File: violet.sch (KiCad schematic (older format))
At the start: 27 parts, among them J1 NEIGHBOR1, J2 NEIGHBOR2, J7 BONUS_ROW

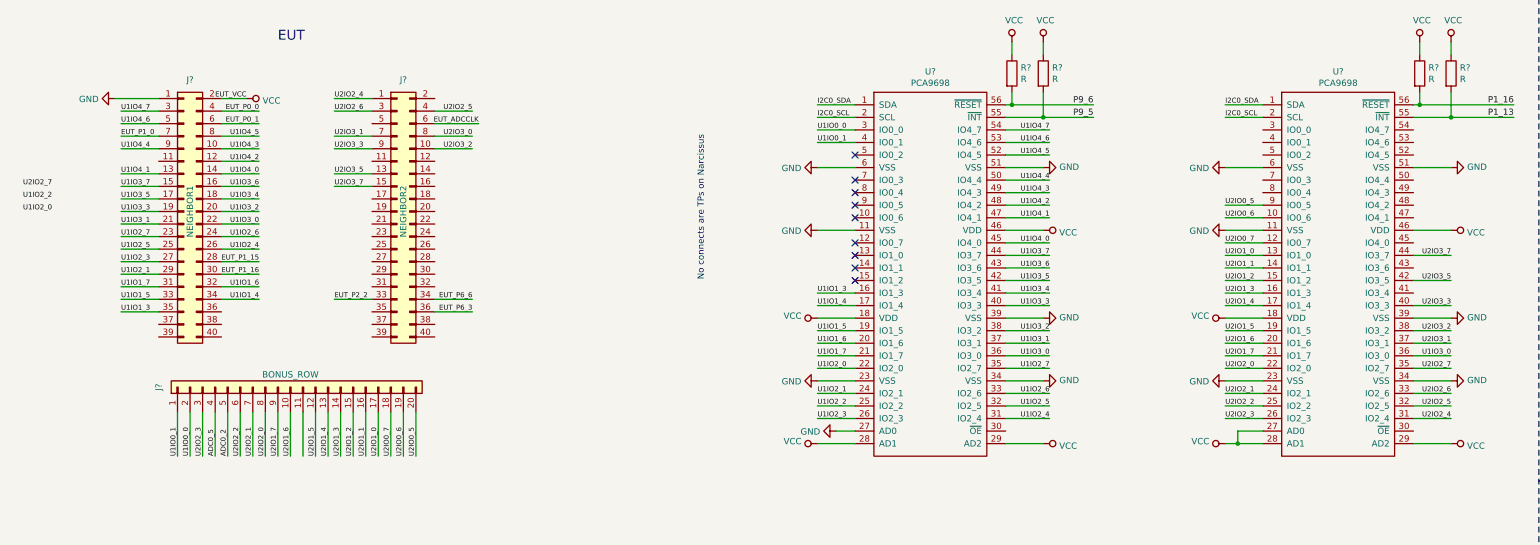
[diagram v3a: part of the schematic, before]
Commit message: Add more labels; fix label nomenclature
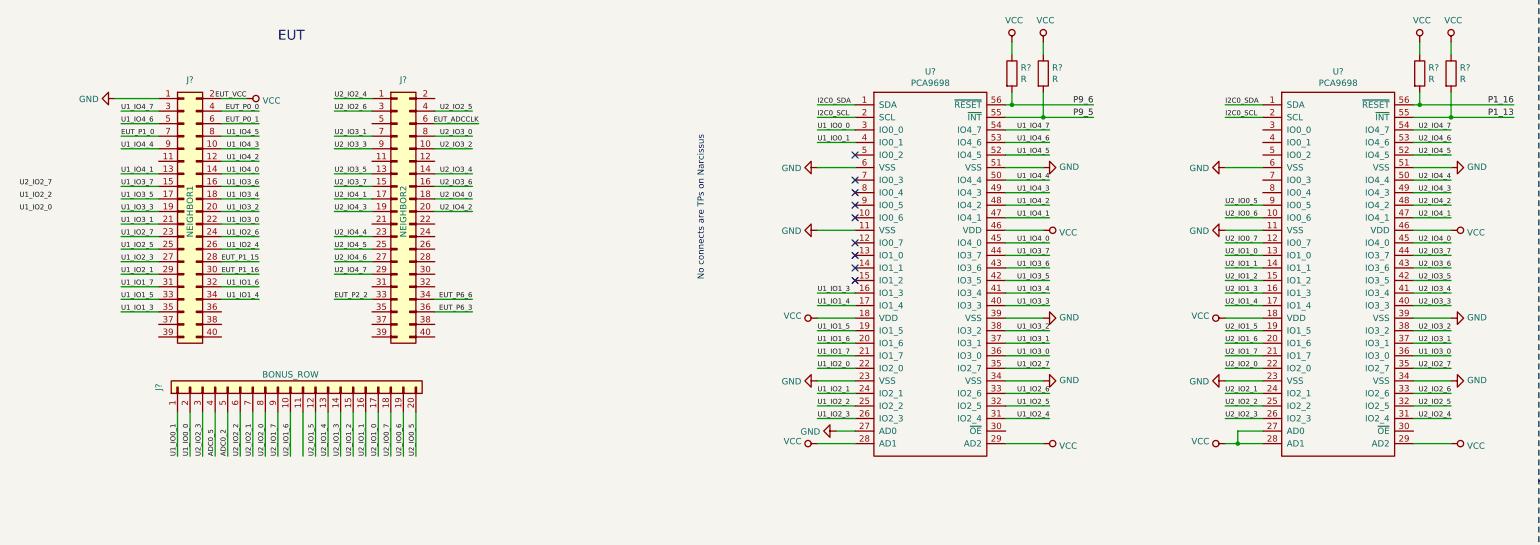
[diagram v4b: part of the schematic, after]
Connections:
- net U2_IO3_4: now reaches J?.14 (Pin_14)
- net U2_IO3_4: now also U?.41 (IO3_4)
- net U2_IO3_6: now reaches J?.16 (Pin_16)
- net U2_IO3_6: now also U?.43 (IO3_6)
- net U2_IO4_1: now reaches J?.17 (Pin_17)
- net U2_IO4_1: now also U?.47 (IO4_1)
- net U2_IO4_0: now reaches J?.18 (Pin_18)
- net U2_IO4_0: now also U?.45 (IO4_0)
- net U2_IO4_3: now reaches J?.19 (Pin_19)
- net U2_IO4_3: now also U?.49 (IO4_3)
- net U2_IO4_2: now reaches J?.20 (Pin_20)
- net U2_IO4_2: now also U?.48 (IO4_2)
- net U2_IO4_4: now reaches J?.23 (Pin_23)
- net U2_IO4_4: now also U?.50 (IO4_4)
- net U2_IO4_5: now reaches J?.25 (Pin_25)
- net U2_IO4_5: now also U?.52 (IO4_5)
- net U2_IO4_6: now reaches J?.27 (Pin_27)
- net U2_IO4_6: now also U?.53 (IO4_6)
- net U2_IO4_7: now reaches J?.29 (Pin_29)
- net U2_IO4_7: now also U?.54 (IO4_7)
- net U1IO0_0 renamed U1_IO0_0
- net U1IO0_1 renamed U1_IO0_1
- net U1IO1_3 renamed U1_IO1_3
- net U1IO1_4 renamed U1_IO1_4
- net U1IO1_5 renamed U1_IO1_5
- net U1IO1_6 renamed U1_IO1_6
- net U1IO1_7 renamed U1_IO1_7
- net U1IO2_0 renamed U1_IO2_0
- net U1IO2_1 renamed U1_IO2_1
- net U1IO2_2 renamed U1_IO2_2
- net U1IO2_3 renamed U1_IO2_3
- net U1IO2_4 renamed U1_IO2_4
- net U1IO2_5 renamed U1_IO2_5
- net U1IO2_6 renamed U1_IO2_6
- net U1IO2_7 renamed U1_IO2_7
- net U1IO3_0 renamed U1_IO3_0
- net U1IO3_1 renamed U1_IO3_1
- net U1IO3_2 renamed U1_IO3_2
- net U1IO3_3 renamed U1_IO3_3
- net U1IO3_4 renamed U1_IO3_4
- net U1IO3_5 renamed U1_IO3_5
- net U1IO3_6 renamed U1_IO3_6
- net U1IO3_7 renamed U1_IO3_7
- net U1IO4_0 renamed U1_IO4_0
- net U1IO4_1 renamed U1_IO4_1
- net U1IO4_2 renamed U1_IO4_2
- net U1IO4_3 renamed U1_IO4_3
- net U1IO4_4 renamed U1_IO4_4
- net U1IO4_5 renamed U1_IO4_5
- net U1IO4_6 renamed U1_IO4_6
- net U1IO4_7 renamed U1_IO4_7
- net U2IO0_5 renamed U2_IO0_5
- net U2IO0_6 renamed U2_IO0_6
- net U2IO0_7 renamed U2_IO0_7
- net U2IO1_0 renamed U2_IO1_0
- net U2IO1_1 renamed U2_IO1_1
- net U2IO1_2 renamed U2_IO1_2
- net U2IO1_3 renamed U2_IO1_3
- net U2IO1_4 renamed U2_IO1_4
- net U2IO1_5 renamed U2_IO1_5
- net U2IO1_6 renamed U2_IO1_6
- net U2IO1_7 renamed U2_IO1_7
- net U2IO2_0 renamed U2_IO2_0
- net U2IO2_1 renamed U2_IO2_1
- net U2IO2_2 renamed U2_IO2_2
- net U2IO2_3 renamed U2_IO2_3
- net U2IO2_4 renamed U2_IO2_4
- net U2IO2_5 renamed U2_IO2_5
- net U2IO2_6 renamed U2_IO2_6
- net U2IO2_7 renamed U2_IO2_7
- net U2IO3_0 renamed U2_IO3_0
- net U2IO3_1 renamed U2_IO3_1
- net U2IO3_2 renamed U2_IO3_2
- net U2IO3_3 renamed U2_IO3_3
- net U2IO3_5 renamed U2_IO3_5
- net U2IO3_7 renamed U2_IO3_7

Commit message: Add more labels; add another I/O expander
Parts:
- added U?: PCA9674, symbol gsg-symbols:PCA9674
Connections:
- net GND: now also U?.2 (AD1), U?.3 (AD2), U?.8 (VSS)
- net I2C0_SCL: now also J?.40 (Pin_40), U?.14 (SCL)
- net I2C0_SDA: now also J?.39 (Pin_39), U?.15 (SDA)
- net U1_IO2_0: now also J?.39 (Pin_39)
- net U1_IO2_2: now also J?.37 (Pin_37)
- net U2_IO2_7: now also J?.28 (Pin_28)
- net VCC: now also U?.1 (AD0)
- net U1_IO0_7: now reaches J?.11 (Pin_11)
- net U1_IO0_7: now also U?.12 (IO0_7)
- net U1_IO1_2: now reaches J?.12 (Pin_12)
- net U1_IO1_2: now also U?.15 (IO1_2)
- net U1_IO1_0: now reaches J?.21 (Pin_21)
- net U1_IO1_0: now also U?.13 (IO1_0)
- net U2_IO0_1: now reaches J?.22 (Pin_22)
- net U2_IO0_1: now also U?.4 (IO0_1)
- net U2_IO0_2: now reaches J?.24 (Pin_24)
- net U2_IO0_2: now also J?.11 (Pin_11), U?.5 (IO0_2)
- net U2_IO0_3: now reaches J?.26 (Pin_26)
- net U2_IO0_3: now also U?.7 (IO0_3)
- net U2_IO0_0: now reaches J?.31 (Pin_31)
- net U2_IO0_0: now also U?.3 (IO0_0)
- net U2_IO0_4: now reaches J?.35 (Pin_35)
- net U2_IO0_4: now also U?.8 (IO0_4)
- net U1_IO1_1: now reaches J?.37 (Pin_37)
- net U1_IO1_1: now also U?.14 (IO1_1)
- net U1_IO0_6: now reaches J?.5 (Pin_5)
- net U1_IO0_6: now also U?.10 (IO0_6)
- net U1_IO0_3: now reaches J?.36 (Pin_36)
- net U1_IO0_3: now also U?.7 (IO0_3)
- net U1_IO0_4: now reaches J?.38 (Pin_38)
- net U1_IO0_4: now also U?.8 (IO0_4)
- net U1_IO0_5: now reaches J?.40 (Pin_40)
- net U1_IO0_5: now also U?.9 (IO0_5)
- net U1_IO0_2: now reaches U?.5 (IO0_2)
- no-connect marks 151 -> 142
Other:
- note removed: "No connects are TPs on Narcissus"
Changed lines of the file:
@@
 	3150 4300 3150 3950
-Wire Wire Line
-	3050 4300 3050 3950
 Wire Wire Line
 	2850 4300 2850 3950
@@
 Wire Wire Line
 	2100 8750 1500 8750
-$Comp
-L gsg-symbols:PCA9698 U?
-U 1 1 5F510C18
-P 8050 2850
-F 0 "U?" H 8050 4465 50  0000 C CNN
-F 1 "PCA9698" H 8050 4374 50  0000 C CNN
-F 2 "" H 8050 2850 40  0000 C CNN
-F 3 "" H 8050 2850 40  0000 C CNN
-	1    8050 2850
-	1    0    0    -1
-$EndComp
 $Comp
 L gsg-symbols:PCA9698 U?
@@
 Text Label 12700 1600 2    50   ~ 0
 P1_13
-NoConn ~ 7450 2700
-NoConn ~ 7450 2600
-NoConn ~ 7450 2400
-NoConn ~ 7450 2100
-NoConn ~ 7450 2300
-NoConn ~ 7450 2900
-NoConn ~ 7450 2800
-NoConn ~ 7450 2200
-NoConn ~ 7450 1900
-Text Notes 6250 2900 1    50   ~ 0
-No connects are TPs on Narcissus
 Text Label 15100 6700 0    40   ~ 0
 P2_8
@@
 Text Label 2700 2650 2    40   ~ 0
 U1_IO2_4
-Text Label 1050 2250 2    40   ~ 0
-U1_IO2_2
-Text Label 1050 2350 2    40   ~ 0
-U1_IO2_0
 Wire Wire Line
 	8650 3600 9000 3600
@@
 Text Label 4400 1550 2    40   ~ 0
 U2_IO2_5
-Text Label 1050 2150 2    40   ~ 0
+Text Label 4400 2750 2    40   ~ 0
 U2_IO2_7
 Wire Wire Line
@@
 Text Label 12200 1700 2    40   ~ 0
 U2_IO4_7
+Text Label 3050 4300 1    50   ~ 0
+I\O
+Text Label 4600 1450 2    40   ~ 0
+EUT_+5V
+Wire Wire Line
+	3300 2950 3600 2950
+Wire Wire Line
+	3300 3150 3600 3150
+Text Label 3300 2950 0    40   ~ 0
+U2_IO0_0
+Text Label 3300 3150 0    40   ~ 0
+U2_IO0_4
+Wire Wire Line
+	10400 1700 10700 1700
+Wire Wire Line
+	10400 1900 10700 1900
+Wire Wire Line
+	10400 2200 10700 2200
+Text Label 10400 1700 0    40   ~ 0
+U2_IO0_0
+Text Label 10400 1900 0    40   ~ 0
+U2_IO0_2
+Text Label 10400 2200 0    40   ~ 0
+U2_IO0_4
+Text Label 4250 2850 0    40   ~ 0
+I\O
+Text Label 4250 2950 0    40   ~ 0
+I\O
+Text Label 4250 3250 0    40   ~ 0
+I\O
+Text Label 3300 3350 0    40   ~ 0
+I2C0_SDA
+Wire Wire Line
+	3600 3350 3300 3350
+Text Label 4400 3350 2    40   ~ 0
+I2C0_SCL
+Wire Wire Line
+	4400 3350 4100 3350
+$Comp
+L power:GND #PWR?
+U 1 1 604CCBF3
+P 11050 5700
+F 0 "#PWR?" H 11050 5450 50  0001 C CNN
+F 1 "GND" V 11055 5572 50  0000 R CNN
+F 2 "" H 11050 5700 50  0001 C CNN
+F 3 "" H 11050 5700 50  0001 C CNN
+	1    11050 5700
+	0    1    1    0
+$EndComp
+Wire Wire Line
+	11350 5700 11050 5700
+Wire Wire Line
+	1600 1950 1900 1950
+Text Label 4400 2650 2    40   ~ 0
+U2_IO0_3
+Text Label 4400 2450 2    40   ~ 0
+U2_IO0_1
+Text Label 1600 3350 0    40   ~ 0
+U1_IO2_0
+Text Label 1600 3250 0    40   ~ 0
+U1_IO2_2
+Text Label 4400 2550 2    40   ~ 0
+U2_IO0_2
+Wire Wire Line
+	1600 3250 1900 3250
+Wire Wire Line
+	1600 3350 1900 3350
+$Comp
+L gsg-symbols:PCA9698 U?
+U 1 1 5F510C18
+P 8050 2850
+F 0 "U?" H 8050 4465 50  0000 C CNN
+F 1 "PCA9698" H 8050 4374 50  0000 C CNN
+F 2 "" H 8050 2850 40  0000 C CNN
+F 3 "" H 8050 2850 40  0000 C CNN
+	1    8050 2850
+	1    0    0    -1
+$EndComp
+Wire Wire Line
+	7150 1900 7450 1900
+Wire Wire Line
+	7150 2100 7450 2100
+Wire Wire Line
+	7150 2200 7450 2200
+Wire Wire Line
+	7150 2300 7450 2300
+Wire Wire Line
+	7150 2400 7450 2400
+Wire Wire Line
+	7150 2600 7450 2600
+Wire Wire Line
+	7150 2700 7450 2700
+Wire Wire Line
+	7150 2800 7450 2800
+Wire Wire Line
+	7150 2900 7450 2900
+Text Label 7150 1900 0    40   ~ 0
+U1_IO0_2
+Text Label 1600 1950 0    40   ~ 0
+U2_IO0_2
+Wire Wire Line
+	2700 3150 2400 3150
+Wire Wire Line
+	2700 3250 2400 3250
+Wire Wire Line
+	2700 3350 2400 3350
+Text Label 7150 2100 0    40   ~ 0
+U1_IO0_3
+Text Label 7150 2200 0    40   ~ 0
+U1_IO0_4
+Text Label 7150 2300 0    40   ~ 0
+U1_IO0_5
+Text Label 2700 3150 2    40   ~ 0
+U1_IO0_3
+Text Label 2700 3250 2    40   ~ 0
+U1_IO0_4
+Text Label 2700 3350 2    40   ~ 0
+U1_IO0_5
+Wire Wire Line
+	3300 1650 3600 1650
+Wire Wire Line
+	3300 1950 3600 1950
+Wire Wire Line
+	3300 2450 3600 2450
+Text Label 7150 2400 0    40   ~ 0
+U1_IO0_6
+Text Label 7150 2600 0    40   ~ 0
+U1_IO0_7
+Text Label 7150 2700 0    40   ~ 0
+U1_IO1_0
+Text Label 3300 1650 0    40   ~ 0
+U1_IO0_6
+Text Label 3300 1950 0    40   ~ 0
+U1_IO0_7
+Text Label 3300 2450 0    40   ~ 0
+U1_IO1_0
+Wire Wire Line
+	3300 3250 3600 3250
+Text Label 7150 2800 0    40   ~ 0
+U1_IO1_1
+Text Label 3300 3250 0    40   ~ 0
+U1_IO1_1
+Wire Wire Line
+	4400 1950 4100 1950
+Text Label 7150 2900 0    40   ~ 0
+U1_IO1_2
+Text Label 4400 1950 2    40   ~ 0
+U1_IO1_2
+Wire Wire Line
+	4400 2450 4100 2450
+Wire Wire Line
+	4400 2550 4100 2550
+Wire Wire Line
+	4400 2650 4100 2650
+Wire Wire Line
+	4400 2750 4100 2750
+Wire Wire Line
+	10400 1800 10700 1800
+Wire Wire Line
+	10400 2100 10700 2100
+Text Label 10400 1800 0    40   ~ 0
+U2_IO0_1
+Text Label 10400 2100 0    40   ~ 0
+U2_IO0_3
+$Comp
+L gsg-symbols:PCA9674 U?
+U 1 1 6124F8C7
+P 11800 5350
+F 0 "U?" H 11800 5902 40  0000 C CNN
+F 1 "PCA9674" H 11800 5826 40  0000 C CNN
+F 2 "" H 11800 5350 40  0000 C CNN
+F 3 "" H 11800 5350 40  0000 C CNN
+	1    11800 5350
+	1    0    0    -1
+$EndComp
+Wire Wire Line
+	12550 5200 12250 5200
+Text Label 12550 5200 2    40   ~ 0
+I2C0_SCL
+Wire Wire Line
+	12250 5100 12550 5100
+Text Label 12550 5100 2    40   ~ 0
+I2C0_SDA
+$Comp
+L power:GND #PWR?
+U 1 1 61412BAB
+P 11050 5200
+F 0 "#PWR?" H 11050 4950 50  0001 C CNN
+F 1 "GND" V 11055 5072 50  0000 R CNN
+F 2 "" H 11050 5200 50  0001 C CNN
+F 3 "" H 11050 5200 50  0001 C CNN
+	1    11050 5200
+	0    1    1    0
+$EndComp
+Wire Wire Line
+	11350 5200 11150 5200
+Wire Wire Line
+	11350 5100 11150 5100
+Wire Wire Line
+	11150 5100 11150 5200
+Connection ~ 11150 5200
+Wire Wire Line
+	11150 5200 11050 5200
+$Comp
+L power:VCC #PWR?
+U 1 1 614CF790
+P 11050 5000
+F 0 "#PWR?" H 11050 4850 50  0001 C CNN
+F 1 "VCC" V 11068 5127 50  0000 L CNN
+F 2 "" H 11050 5000 50  0001 C CNN
+F 3 "" H 11050 5000 50  0001 C CNN
+	1    11050 5000
+	0    -1   -1   0
+$EndComp
+Wire Wire Line
+	11350 5000 11050 5000
 $EndSCHEMATC

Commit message: Add remaining labels; configure third I/O expander; add decoupling caps
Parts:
- added C? (x7): C, symbol Device:C
- added R? (x3): R, symbol Device:R
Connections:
- net GND: now also C?.1, C?.2, C?.2, C?.2, C?.2, C?.2, C?.2
- net P1_11: now also U?.30 (~OE~), R?.2
- net P1_15: now also U?.13 (INT), R?.2
- net P1_17: now also U?.30 (~OE~), R?.2
- net VCC: now also U?.16 (VDD), C?.1, C?.1, C?.1, C?.1, C?.1, C?.1, C?.2, R?.1, R?.1, R?.1
- net U3_IO_P4: now reaches J?.2 (Pin_2)
- net U3_IO_P4: now also U?.9 (P4)
- net U3_IO_P0: now reaches J?.30 (Pin_30)
- net U3_IO_P0: now also U?.4 (P0)
- net U3_IO_P1: now reaches J?.32 (Pin_32)
- net U3_IO_P1: now also U?.5 (P1)
- net U3_IO_P2: now reaches J?.38 (Pin_38)
- net U3_IO_P2: now also U?.6 (P2)
- net U3_IO_P3: now reaches J?.11 (Pin_11)
- net U3_IO_P3: now also U?.7 (P3)
- no-connect marks 142 -> 168
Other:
- note added: "???"
- moved on the sheet: R?, U?

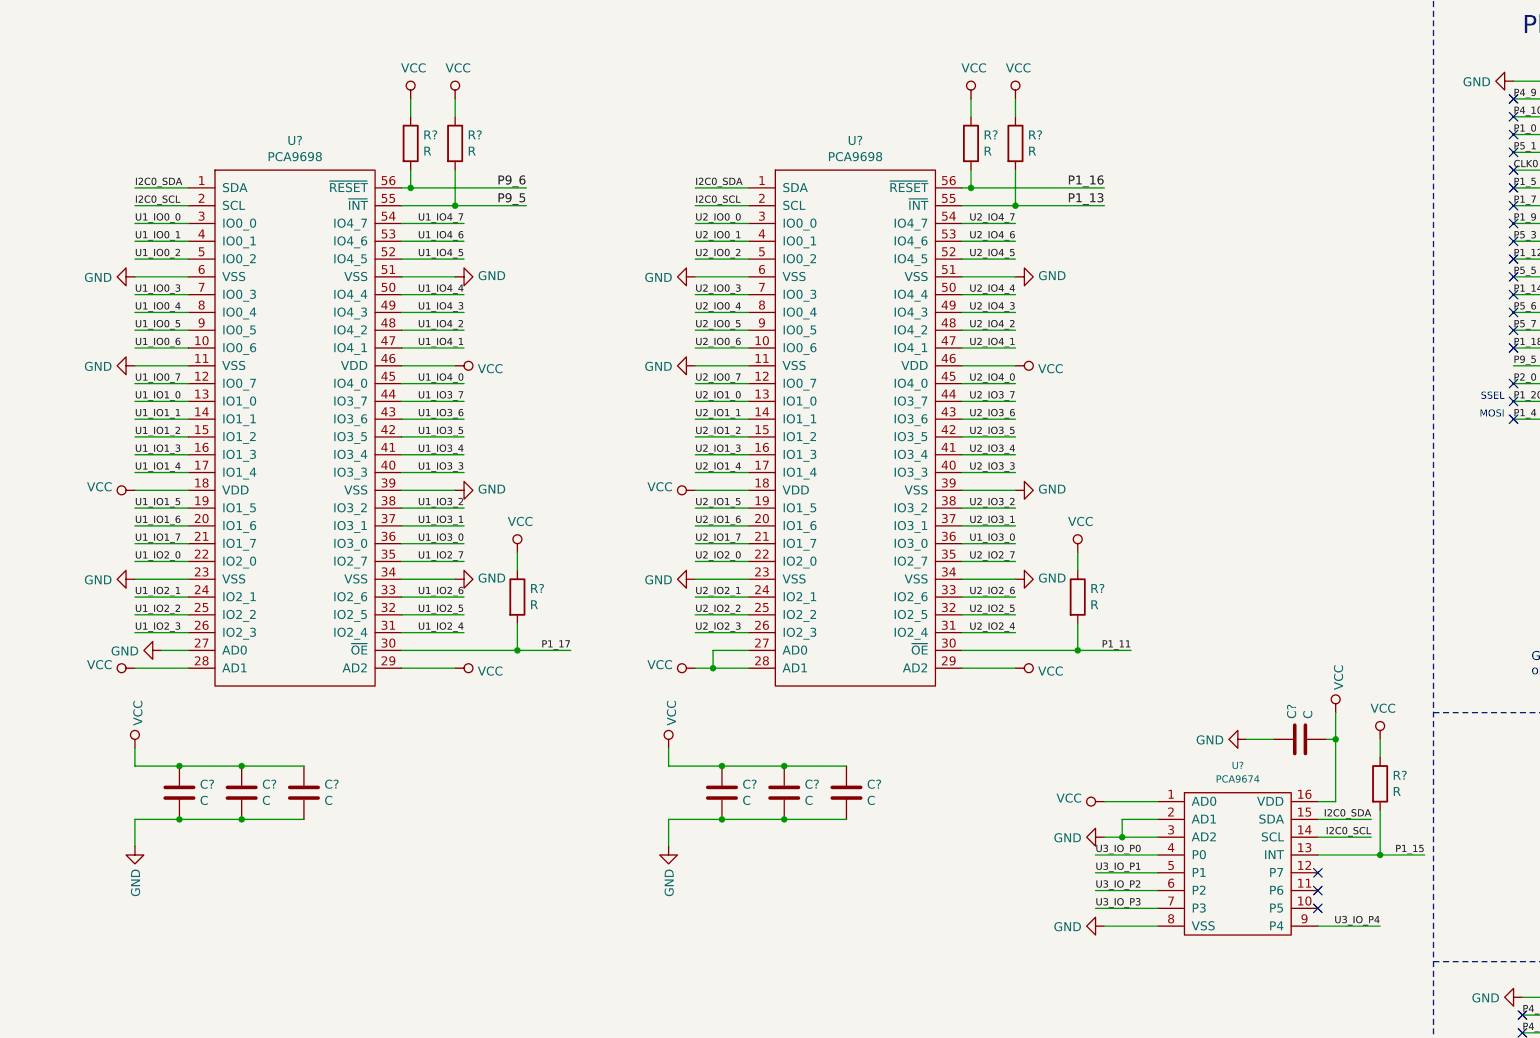
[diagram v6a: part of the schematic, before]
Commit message: Add parts and footprints
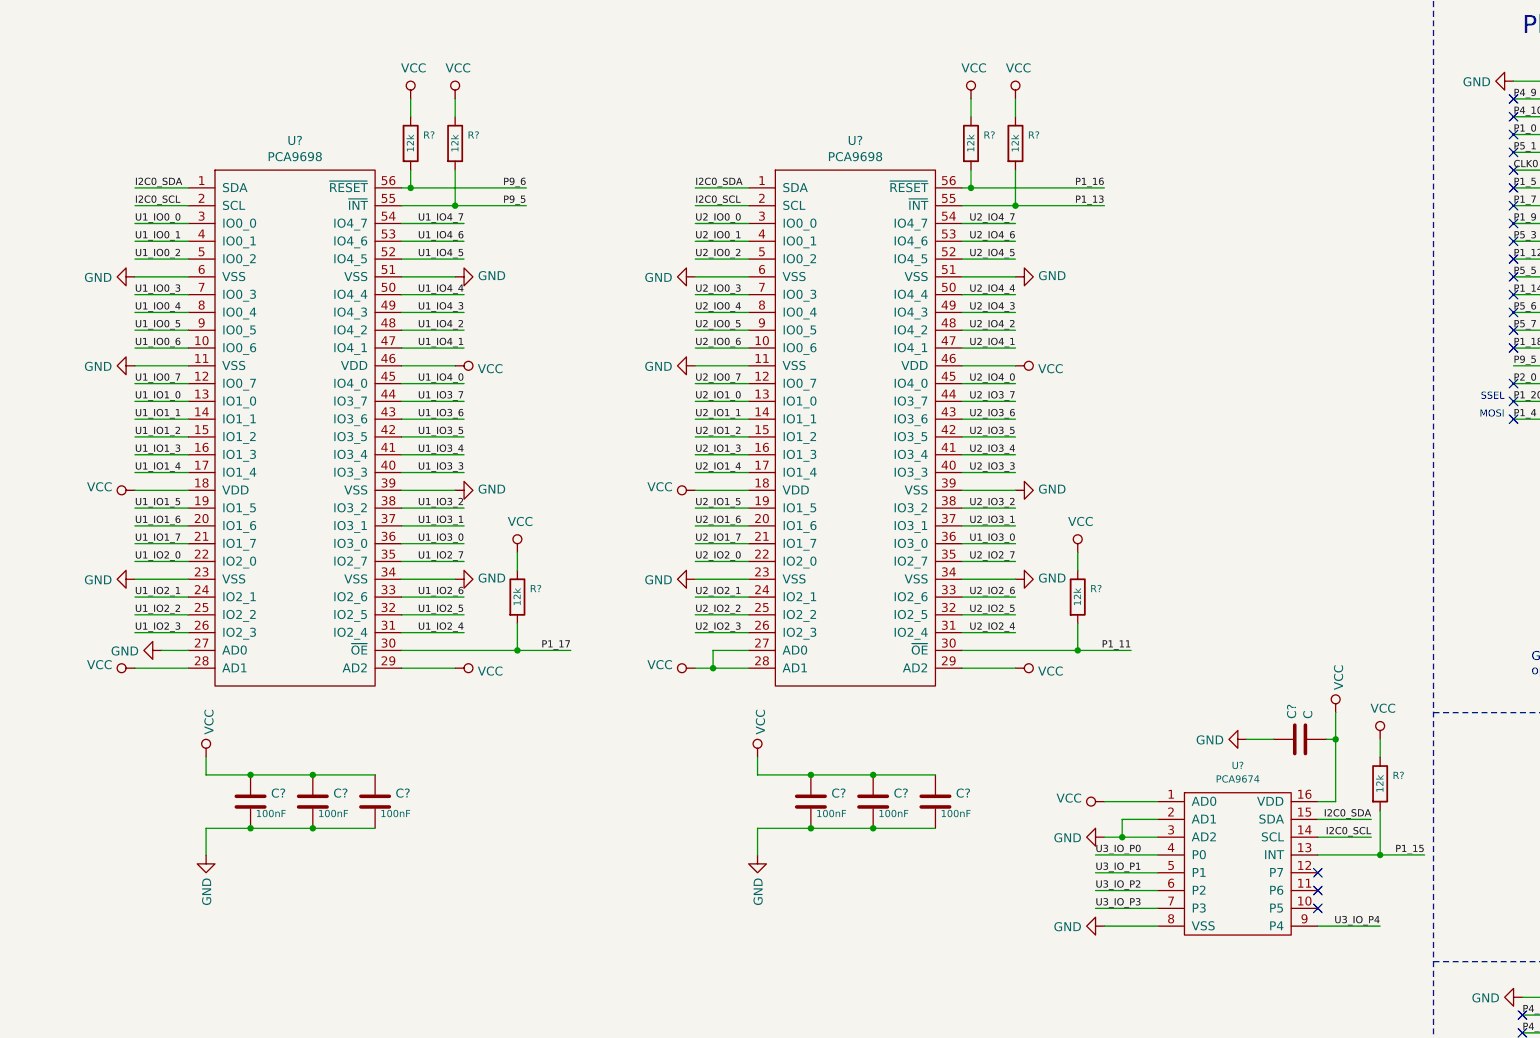
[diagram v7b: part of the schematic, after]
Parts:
- removed C? (x5): C, symbol Device:C
- removed R? (x6): R, symbol Device:R
- added C? (x5): 100nF, gsg-modules:0603, symbol Device:C
- added R? (x6): 12k, gsg-modules:0603, symbol Device:R
- C?: value C -> 100nF; footprint (none) -> gsg-modules:0603; Description (none) -> CAP CER 0.1UF 16V X7R 0603; Manufacturer (none) -> KEMET; Part Number (none) -> C0603C104M4RACTU
- R?: value R -> 12k; footprint (none) -> gsg-modules:0603; Description (none) -> RES 12K OHM 1% 1/10W 0603; Manufacturer (none) -> Stackpole; Part Number (none) -> RMCF0603FT12K0
- U? (x2): footprint (none) -> gsg-modules:TSSOP56; Description (none) -> IC I/O EXPANDER I2C 40B 56TSSOP; Manufacturer (none) -> NXP; Part Number (none) -> PCA9698DGG,512
- U?: footprint (none) -> gsg-modules:TSSOP16; Description (none) -> IC I/O EXPANDER I2C 8B 16TSSOP; Manufacturer (none) -> NXP; Part Number (none) -> PCA9674PW,118
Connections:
- net GND: now also C?.2, C?.2, C?.2, C?.2, C?.2
- net P1_11: now also R?.2
- net P1_13: now also R?.2
- net P1_15: now also R?.2
- net P1_16: now also R?.2
- net P1_17: now also R?.2
- net P9_5: now also R?.2
- net VCC: now also C?.1, C?.1, C?.1, C?.1, C?.1, R?.1, R?.1, R?.1, R?.1, R?.1, R?.1
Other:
- moved on the sheet: C?

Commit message: Annotate schematic symbols
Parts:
- gave numbers to parts that had none: 31
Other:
- moved on the sheet: C10, C8, C9, R10, R8, R9, U4, U5
